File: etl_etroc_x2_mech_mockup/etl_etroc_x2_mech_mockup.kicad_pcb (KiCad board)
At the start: 2 copper layers, 41.7 x 22.3 mm, 9 parts, among them J1 Conn_2Rows-47Pins, J2 Conn_2Rows-47Pins, J3 Conn_2Rows-47Pins, J4 Conn_2Rows-47Pins

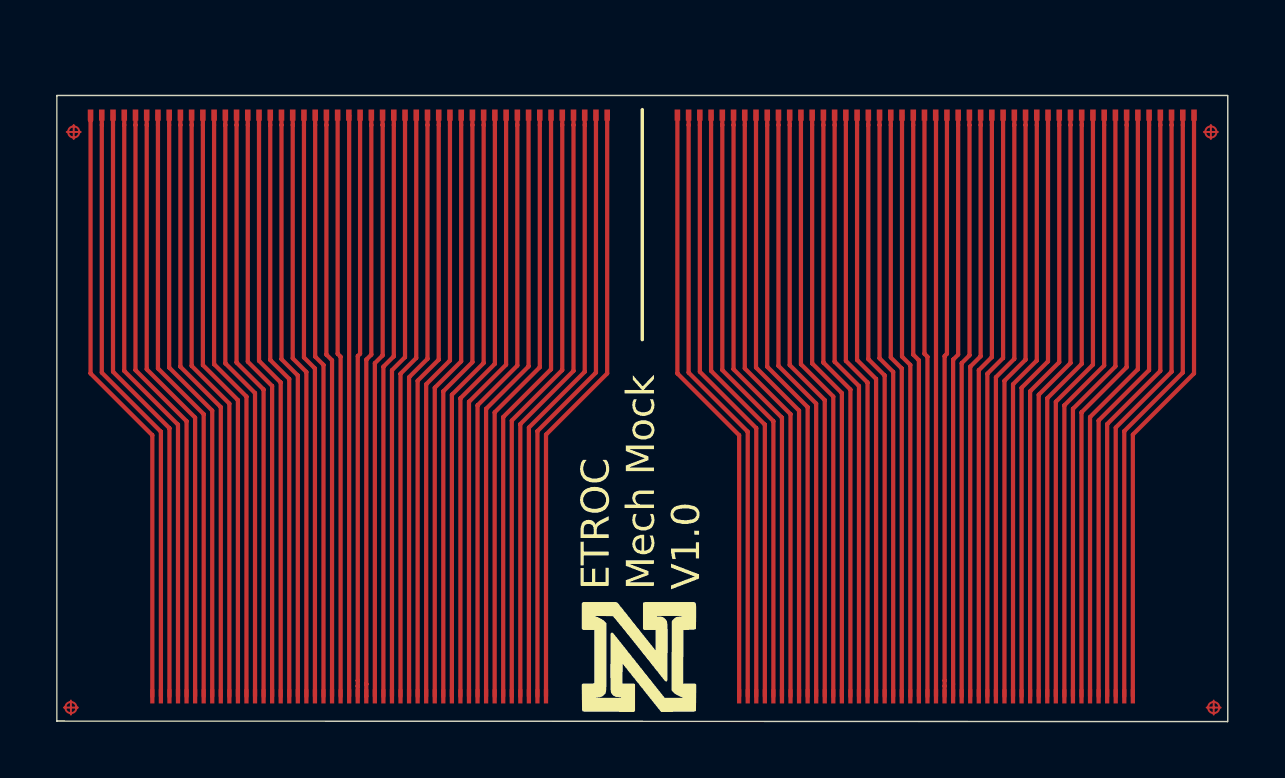
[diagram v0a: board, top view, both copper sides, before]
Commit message: Updates pad number and dimensions on etl_etroc_x2_mech_mockup
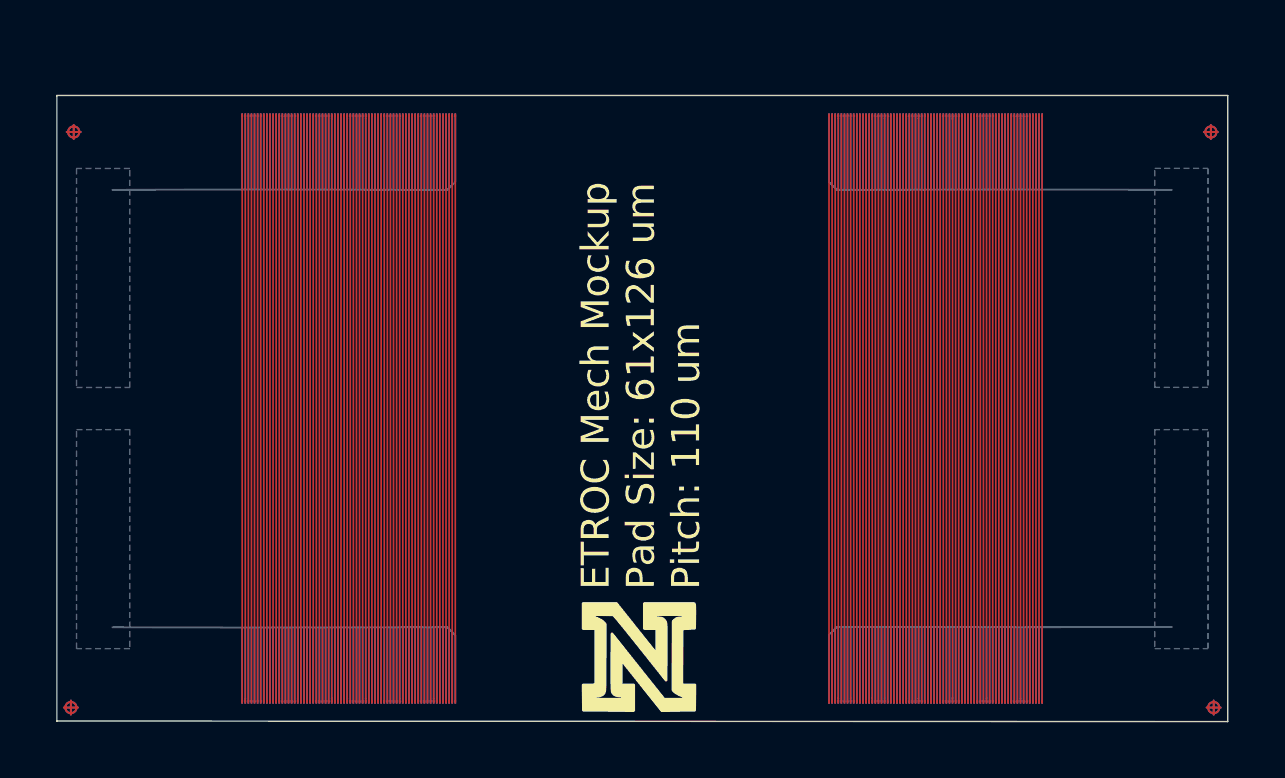
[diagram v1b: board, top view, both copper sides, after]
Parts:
- added J5: Conn_02x35_Top_Bottom, unl_silab:ETROC_70pad_61x126um_110um_pitch, B.Cu at (84.4, 72.0)
- added J6: Conn_02x35_Top_Bottom, unl_silab:ETROC_70pad_61x126um_110um_pitch, B.Cu at (84.4, 92.9)
- added J7: Conn_02x35_Top_Bottom, unl_silab:ETROC_70pad_61x126um_110um_pitch, B.Cu at (105.3, 92.9)
- added J8: Conn_02x35_Top_Bottom, unl_silab:ETROC_70pad_61x126um_110um_pitch, B.Cu at (105.3, 72.0)
- added REF**: crossed_circle_fiducial, unl_silab:crossed_circle_fiducial, B.Cu at (119.0, 93.1)
- added REF**: crossed_circle_fiducial, unl_silab:crossed_circle_fiducial, B.Cu at (118.9, 72.6)
- added REF**: crossed_circle_fiducial, unl_silab:crossed_circle_fiducial, B.Cu at (78.4, 72.6)
- added REF**: crossed_circle_fiducial, unl_silab:crossed_circle_fiducial, B.Cu at (78.3, 93.1)
- J1, J2: value Conn_2Rows-47Pins -> Conn_02x35_Top_Bottom; footprint unl_silab:etroc_mockup_wirebond_pads -> unl_silab:ETROC_70pad_61x126um_110um_pitch
- J3, J4: value Conn_2Rows-47Pins -> Conn_02x35_Top_Bottom; footprint unl_silab:ETROC -> unl_silab:ETROC_70pad_61x126um_110um_pitch
- moved J4 33.6 mm to (105.3, 92.9)
- moved J2 31.8 mm to (105.3, 72.0)
- moved J1 17.7 mm to (84.4, 92.9)
- moved J3 15.5 mm to (84.4, 72.0)
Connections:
- net /A1 renamed /TOP_A1
- net /A10 renamed /TOP_A10
- net /A11 renamed /TOP_A11
- net /A12 renamed /TOP_A12
- net /A13 renamed /TOP_A13
- net /A14 renamed /TOP_A14
- net /A15 renamed /TOP_A15
- net /A16 renamed /TOP_A16
- net /A17 renamed /TOP_A17
- net /A18 renamed /TOP_A18
- net /A19 renamed /TOP_A19
- net /A2 renamed /TOP_A2
- net /A20 renamed /TOP_A20
- net /A21 renamed /TOP_A21
- net /A22 renamed /TOP_A22
- net /A23 renamed /TOP_A23
- net /A24 renamed /TOP_A24
- net /A25 renamed /TOP_A25
- net /A26 renamed /TOP_A26
- net /A27 renamed /TOP_A27
- net /A28 renamed /TOP_A28
- net /A29 renamed /TOP_A29
- net /A3 renamed /TOP_A3
- net /A30 renamed /TOP_A30
- net /A31 renamed /TOP_A31
- net /A32 renamed /TOP_A32
- net /A33 renamed /TOP_A33
- net /A34 renamed /TOP_A34
- net /A35 renamed /TOP_A35
- net /A36 renamed /TOP_A36
- net /A37 renamed /TOP_A37
- net /A38 renamed /TOP_A38
- net /A39 renamed /TOP_A39
- net /A4 renamed /TOP_A4
- net /A40 renamed /TOP_A40
- net /A41 renamed /TOP_A41
- net /A42 renamed /TOP_A42
- net /A43 renamed /TOP_A43
- net /A44 renamed /TOP_A44
- net /A45 renamed /TOP_A45
- net /A46 renamed /TOP_A46
- net /A47 renamed /TOP_A47
- net /A5 renamed /TOP_A5
- net /A6 renamed /TOP_A6
- net /A7 renamed /TOP_A7
- net /A8 renamed /TOP_A8
- net /A9 renamed /TOP_A9
- net /B1 renamed /TOP_B1
- net /B10 renamed /TOP_B10
- net /B11 renamed /TOP_B11
- net /B12 renamed /TOP_B12
- net /B13 renamed /TOP_B13
- net /B14 renamed /TOP_B14
- net /B15 renamed /TOP_B15
- net /B16 renamed /TOP_B16
- net /B17 renamed /TOP_B17
- net /B18 renamed /TOP_B18
- net /B19 renamed /TOP_B19
- net /B2 renamed /TOP_B2
- net /B20 renamed /TOP_B20
- net /B21 renamed /TOP_B21
- net /B22 renamed /TOP_B22
- net /B23 renamed /TOP_B23
- net /B24 renamed /TOP_B24
- net /B25 renamed /TOP_B25
- net /B26 renamed /TOP_B26
- net /B27 renamed /TOP_B27
- net /B28 renamed /TOP_B28
- net /B29 renamed /TOP_B29
- net /B3 renamed /TOP_B3
- net /B30 renamed /TOP_B30
- net /B31 renamed /TOP_B31
- net /B32 renamed /TOP_B32
- net /B33 renamed /TOP_B33
- net /B34 renamed /TOP_B34
- net /B35 renamed /TOP_B35
- net /B36 renamed /TOP_B36
- net /B37 renamed /TOP_B37
- net /B38 renamed /TOP_B38
- net /B39 renamed /TOP_B39
- net /B4 renamed /TOP_B4
- net /B40 renamed /TOP_B40
- net /B41 renamed /TOP_B41
- net /B42 renamed /TOP_B42
- net /B43 renamed /TOP_B43
- net /B44 renamed /TOP_B44
- net /B45 renamed /TOP_B45
- net /B46 renamed /TOP_B46
- net /B47 renamed /TOP_B47
- net /B5 renamed /TOP_B5
- net /B6 renamed /TOP_B6
- net /B7 renamed /TOP_B7
- net /B8 renamed /TOP_B8
- net /B9 renamed /TOP_B9
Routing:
- net /BOT_GRP2: track 0.00 -> 198.3 mm
- net /BOT_GRP4: track 0.00 -> 198.3 mm
- net /BOT_GRP3: track 0.00 -> 198.3 mm
- net /BOT_GRP1: track 0.00 -> 198.3 mm
- net /TOP_B70: track 0.00 -> 20.9 mm
- net /TOP_B67: track 0.00 -> 20.9 mm
- net /TOP_B66: track 0.00 -> 20.9 mm
- net /TOP_B62: track 0.00 -> 20.9 mm
- net /TOP_B61: track 0.00 -> 20.9 mm
- net /TOP_B60: track 0.00 -> 20.9 mm
- net /TOP_B59: track 0.00 -> 20.9 mm
- net /TOP_B56: track 0.00 -> 20.9 mm
- net /TOP_B55: track 0.00 -> 20.9 mm
- net /TOP_B51: track 0.00 -> 20.9 mm
- net /TOP_B50: track 0.00 -> 20.9 mm
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- added copper zone on B.Cu, net /BOT_GRP1
- added copper zone on B.Cu, net /BOT_GRP2
- added copper zone on B.Cu, net /BOT_GRP3
- added copper zone on B.Cu, net /BOT_GRP4
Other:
- net class Default: clearance 0.152 -> 0.04; trace_width 0.152 -> 0.061
- rule trace_clearance: 0.152 -> 0.04
- rule trace_min: 0.15 -> 0.05
- board text added: "ETROC Mech Mockup Pad Size: 61x126 um Pitch: 110 um"
- board text removed: "ETROC Mech Mock V1.0"
